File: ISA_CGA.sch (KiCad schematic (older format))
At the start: 32 parts, among them U1 74S112, U11 74LS74, U12 74LS393, U13 74LS08, U14 74LS32, U15 74LS00, U16 74LS04, U2 74LS74, U20 74LS04, U22 74LS51, U23 74LS32, U24 74LS244, U25 74LS00, U26 74S04, U27 74LS51, U28 74LS10, U29 74S04, U3 74S86, U30 74LS32, U31 74S08, U41 74LS08, U42 74LS86, U43 74S74, U44 74S74, U46 74LS00, U47 74LS51, U48 74LS51, U49 74LS02, U6 74LS04, U62 74LS125, U65 74LS02, U68 74LS86

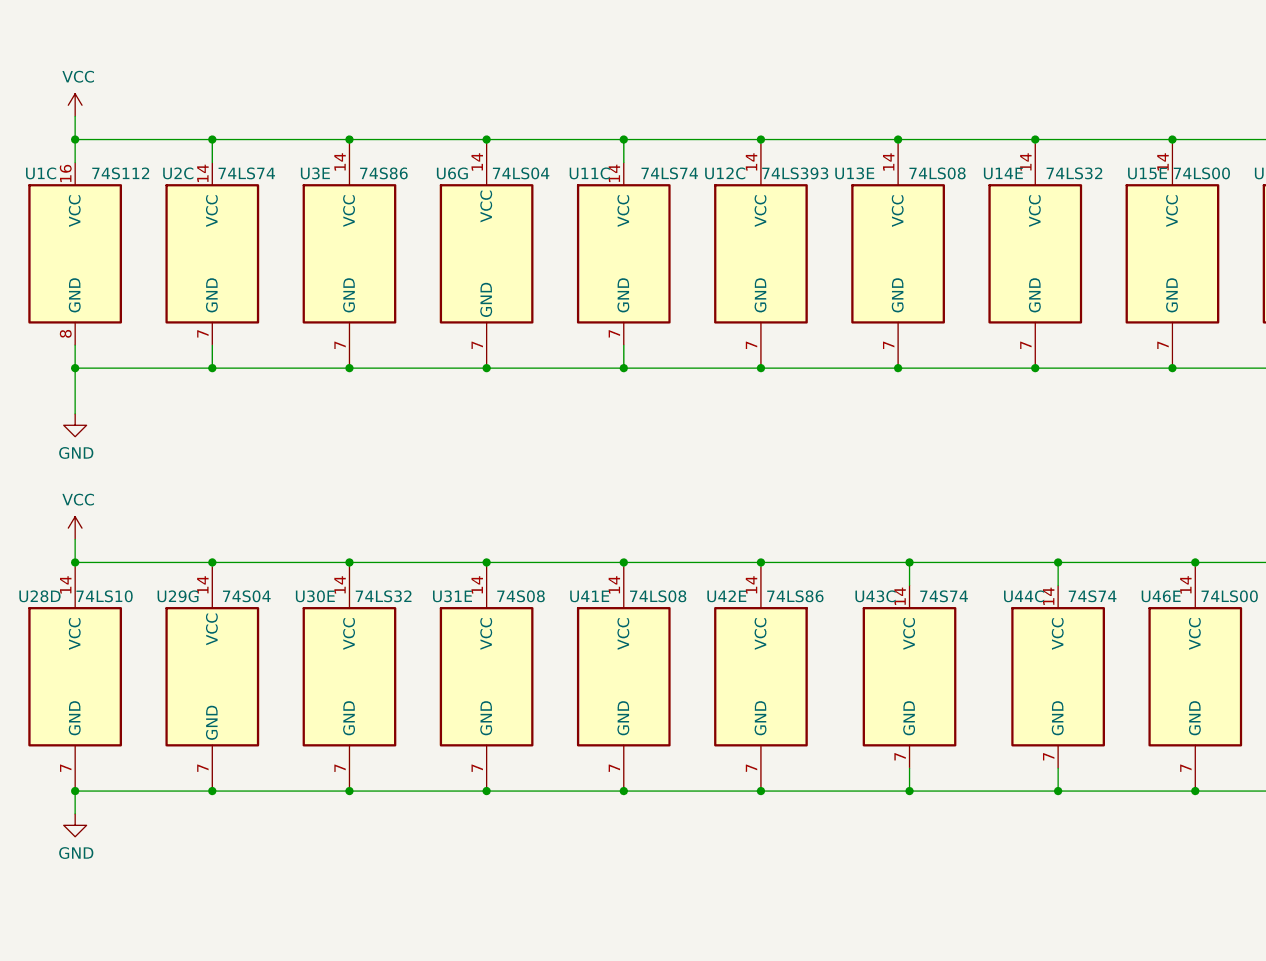
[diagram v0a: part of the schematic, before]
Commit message: Change IC type and add note
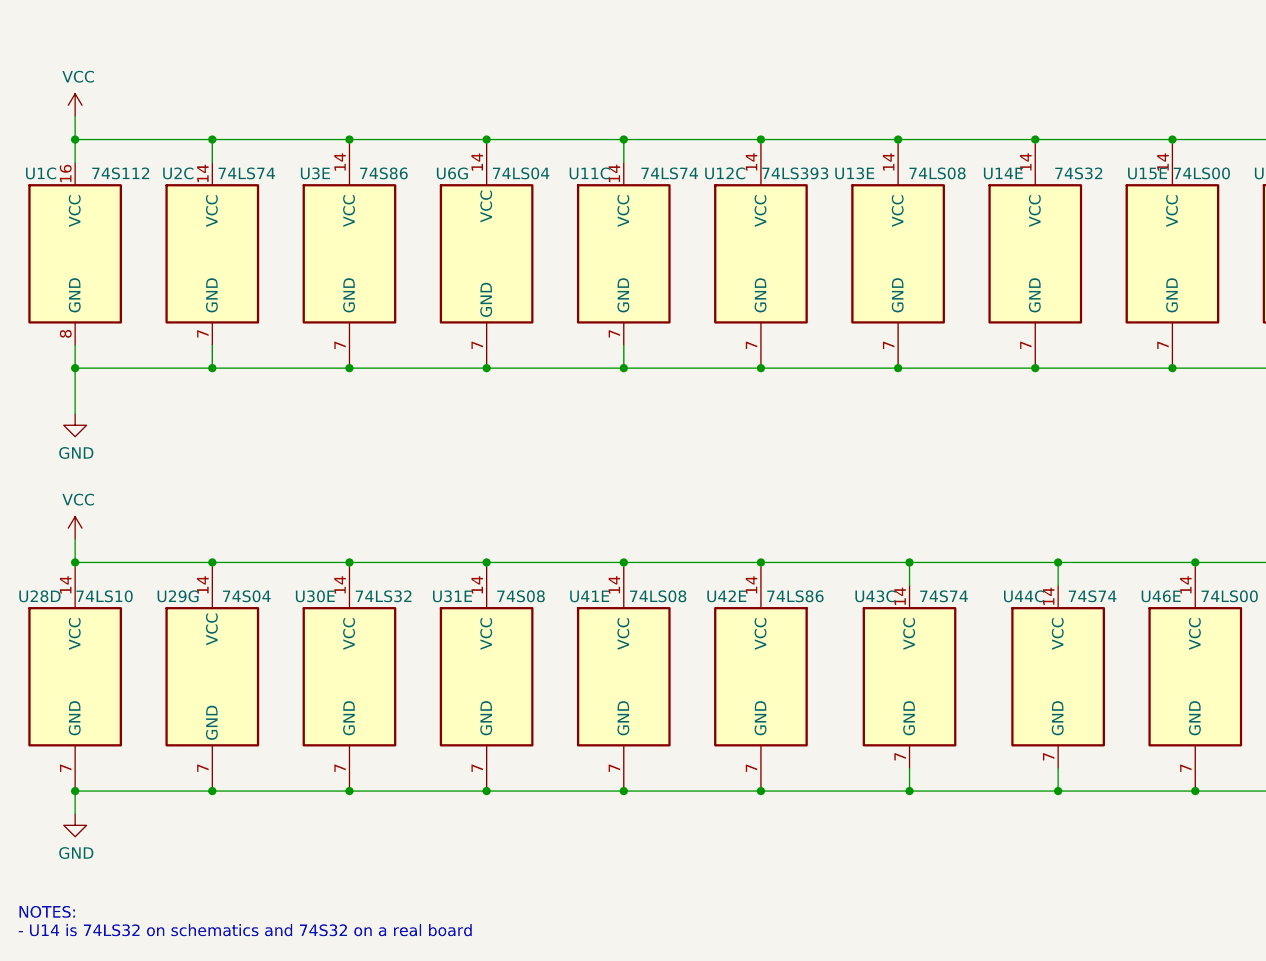
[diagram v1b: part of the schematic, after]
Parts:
- U14: value 74LS32 -> 74S32
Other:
- note added: "NOTES:\n- U14 is 74LS32 on schematics and 74S32 on a real board"
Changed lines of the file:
@@
 AR Path="/607513C2" Ref="U14"  Part="5"
 F 0 "U14" H 5050 3700 50  0000 R CNN
-F 1 "74LS32" H 5400 3700 50  0000 R CNN
+F 1 "74S32" H 5400 3700 50  0000 R CNN
 F 2 "Package_DIP:DIP-14_W7.62mm_LongPads" H 5100 3350 50  0001 C CNN
 F 3 "http://www.ti.com/lit/gpn/sn74LS32" H 5100 3350 50  0001 C CNN
@@
 Wire Wire Line
 	6400 5700 7000 5700
+Text Notes 650  6350 0    50   ~ 0
+NOTES:\n- U14 is 74LS32 on schematics and 74S32 on a real board
 $EndSCHEMATC

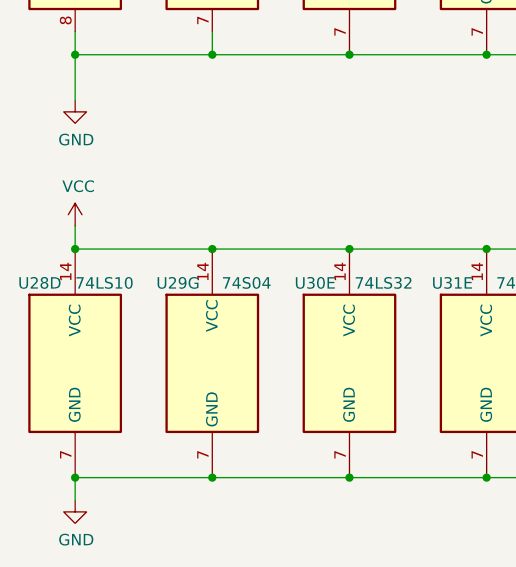
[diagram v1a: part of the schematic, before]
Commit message: U28 is 74S10 and not 74LS10 in original board
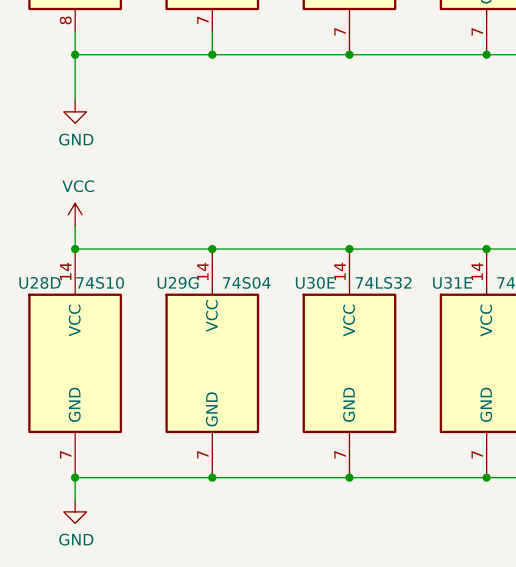
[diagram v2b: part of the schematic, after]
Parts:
- U28: value 74LS10 -> 74S10
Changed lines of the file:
@@
 AR Path="/6073B547" Ref="U28"  Part="4"
 F 0 "U28" H 650 5550 50  0000 L CNN
-F 1 "74LS10" H 900 5550 50  0000 L CNN
+F 1 "74S10" H 900 5550 50  0000 L CNN
 F 2 "Package_DIP:DIP-14_W7.62mm_LongPads" H 900 5200 50  0001 C CNN
 F 3 "http://www.ti.com/lit/gpn/sn74LS10" H 900 5200 50  0001 C CNN
